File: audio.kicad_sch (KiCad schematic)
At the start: 51 parts, among them J10 Earth, J4 NCJ6FA-H-0, J5 NCJ6FA-H-0, J6 Conn_01x04_Pin, J7 Earth, J8 NCJ6FA-H-0, J9 NCJ6FA-H-0, U5 THAT1246, U6 THAT1246, U7 THAT1646, U8 THAT1646

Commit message: add placement notes into the schematic
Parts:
- D3, D4: Placement (none) -> Near Daisy Seed input. Bottom diode to digital ground.
- JP1: Placement (none) -> As close as possible to Daisy Seed AGND/DGND pins.
- R19, R20: Placement (none) -> In signal path between THAT1246 output and protection diode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
- R21, R23: Placement (none) -> Near 2.5V bias junction, close to signal path.
- R22, R24: Placement (none) -> Near 2.5V bias junction. Bottom resistor, connect to analog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
- R25, R26: Placement (none) -> After 1.2k series resistor in signal path. Ground to analog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
- S1: Placement (none) -> Panel-mounted. Route to signal path with short traces, anal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
- U5, U6: Placement (none) -> Near input connector. Pins 1,4 to analog ground, keep groun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
- U7, U8: Placement (none) -> Near output connector. Analog ground reference.
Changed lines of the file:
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@@
 			)
 		)
+		(property "Placement" "Near Daisy Seed input. Bottom diode to digital ground."
+			(at 118.11 69.85 0)
+			(effects
+				(font
+					(size 1.27 1.27)
+				)
+				(hide yes)
+			)
+		)
 		(pin "1"
 		)
@@
 			)
 		)
+		(property "Placement" "After 1.2k series resistor in signal path. Ground to analog ground."
+			(at 121.92 115.57 0)
+			(effects
+				(font
+					(size 1.27 1.27)
+				)
+				(hide yes)
+			)
+		)
 		(pin "1"
 		)
@@
 			)
 		)
+		(property "Placement" "Near 2.5V bias junction, close to signal path."
+			(at 111.76 60.96 0)
+			(effects
+				(font
+					(size 1.27 1.27)
+				)
+				(hide yes)
+			)
+		)
 		(pin "1"
 		)
@@
 			)
 		)
+		(property "Placement" "Panel-mounted. Route to signal path with short traces, analog ground."
+			(at 86.36 100.33 0)
+			(effects
+				(font
+					(size 1.27 1.27)
+				)
+				(hide yes)
+			)
+		)
 		(pin "1"
 		)
@@
 			)
 		)
+		(property "Placement" "As close as possible to Daisy Seed AGND/DGND pins."
+			(at 229.87 138.43 0)
+			(effects
+				(font
+					(size 1.27 1.27)
+				)
+				(hide yes)
+			)
+		)
 		(pin "2"
 		)
@@
 			)
 		)
+		(property "Placement" "Near input connector. Pins 1,4 to analog ground, keep ground path short and clean."
+			(at 58.42 107.95 0)
+			(effects
+				(font
+					(size 1.27 1.27)
+				)
+				(hide yes)
+			)
+		)
 		(pin "1"
 		)
@@
 			)
 		)
+		(property "Placement" "Near output connector. Analog ground reference."
+			(at 205.74 102.87 0)
+			(effects
+				(font
+					(size 1.27 1.27)
+				)
+				(hide yes)
+			)
+		)
 		(pin "1"
 		)
@@
 			)
 		)
+		(property "Placement" "Near 2.5V bias junction, close to signal path."
+			(at 105.41 60.96 0)
+			(effects
+				(font
+					(size 1.27 1.27)
+				)
+				(hide yes)
+			)
+		)
 		(pin "1"
 		)
@@
 			)
 		)
+		(property "Placement" "Near 2.5V bias junction. Bottom resistor, connect to analog ground."
+			(at 105.41 83.82 0)
+			(effects
+				(font
+					(size 1.27 1.27)
+				)
+				(hide yes)
+			)
+		)
 		(pin "1"
 		)
@@
 			)
 		)
+		(property "Placement" "Near input connector. Pins 1,4 to analog ground, keep ground path short and clean."
+			(at 58.42 45.72 0)
+			(effects
+				(font
+					(size 1.27 1.27)
+				)
+				(hide yes)
+			)
+		)
 		(pin "1"
 		)
@@
 			)
 		)
+		(property "Placement" "Near output connector. Analog ground reference."
+			(at 205.74 40.64 0)
+			(effects
+				(font
+					(size 1.27 1.27)
+				)
+				(hide yes)
+			)
+		)
 		(pin "1"
 		)
@@
 			)
 		)
+		(property "Placement" "In signal path between THAT1246 output and protection diodes."
+			(at 81.28 69.85 0)
+			(effects
+				(font
+					(size 1.27 1.27)
+				)
+				(hide yes)
+			)
+		)
 		(pin "1"
 		)
@@
 			)
 		)
+		(property "Placement" "In signal path between THAT1246 output and protection diodes."
+			(at 81.28 74.93 0)
+			(effects
+				(font
+					(size 1.27 1.27)
+				)
+				(hide yes)
+			)
+		)
 		(pin "1"
 		)
@@
 			)
 		)
+		(property "Placement" "After 1.2k series resistor in signal path. Ground to analog ground."
+			(at 121.92 102.87 0)
+			(effects
+				(font
+					(size 1.27 1.27)
+				)
+				(hide yes)
+			)
+		)
 		(pin "1"
 		)
@@
 			)
 		)
+		(property "Placement" "Near 2.5V bias junction. Bottom resistor, connect to analog ground."
+			(at 111.76 83.82 0)
+			(effects
+				(font
+					(size 1.27 1.27)
+				)
+				(hide yes)
+			)
+		)
 		(pin "1"
 		)
@@
 			(at 125.73 74.93 0)
 			(effects
+				(font
+					(size 1.27 1.27)
+				)
+				(hide yes)
+			)
+		)
+		(property "Placement" "Near Daisy Seed input. Bottom diode to digital ground."
+			(at 125.73 74.93 0)
+			(effects

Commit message: dealing with protection circuit changes
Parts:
- D4: renamed from D3; value BAT54S -> BAV99; symbol Diode:BAT54S -> Diode:BAV99
- D5: renamed from D4; value BAT54S -> BAV99; symbol Diode:BAT54S -> Diode:BAV99
- renumbered D9 to D10, D10 to D11, D11 to D12, D12 to D13, D5 to D6, D6 to D7, D7 to D8, D8 to D9, J9 to J10, J10 to J8, J8 to J9
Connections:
- net AUDIO_IN_L: no longer D4.3 (COM)
- net AUDIO_IN_R: no longer D5.3 (COM)

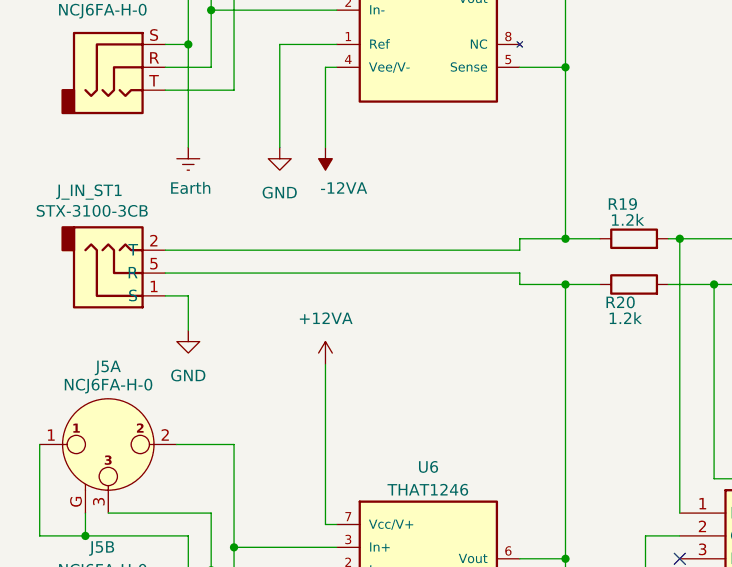
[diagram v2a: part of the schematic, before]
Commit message: deleted 3.55mm input jacks
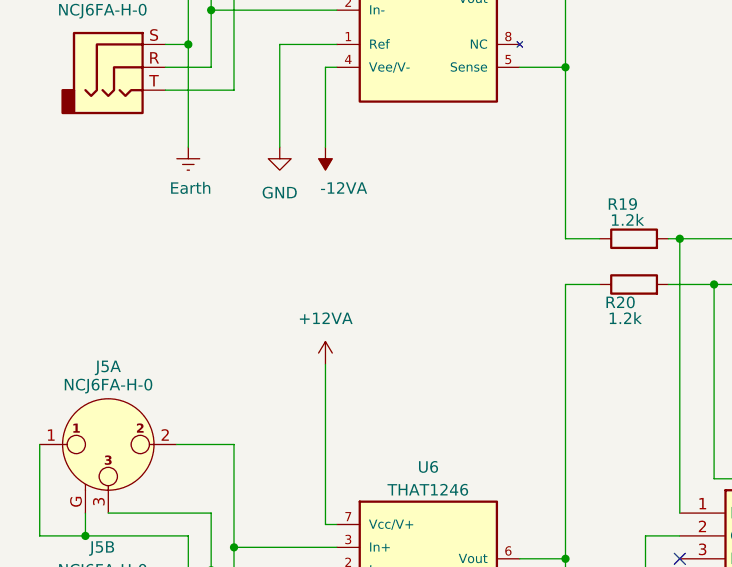
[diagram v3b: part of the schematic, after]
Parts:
- removed J_IN_ST1: STX-3100-3CB, Connector_Audio:Jack_3.5mm_Kycon_STX-3100-3CB, symbol Connector_Audio:AudioJack3
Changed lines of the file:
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@@
 	)
 	(junction
-		(at 73.66 74.93)
-		(diameter 0)
-		(color 0 0 0 0)
-	)
-	(junction
 		(at 184.15 69.85)
 		(diameter 0)
@@
 	)
 	(junction
-		(at 73.66 69.85)
-		(diameter 0)
-		(color 0 0 0 0)
-	)
-	(junction
 		(at 231.14 46.99)
 		(diameter 0)
@@
 	(wire
 		(pts
-			(xy 68.58 69.85) (xy 73.66 69.85)
-		)
-		(stroke
-			(width 0)
-			(type default)
-		)
-	)
-	(wire
-		(pts
 			(xy 43.18 110.49) (xy 43.18 121.92)
 		)
@@
 	(wire
 		(pts
-			(xy 31.75 76.2) (xy 31.75 80.01)
-		)
-		(stroke
-			(width 0)
-			(type default)
-		)
-	)
-	(wire
-		(pts
 			(xy 184.15 41.91) (xy 195.58 41.91)
 		)
@@
 	(wire
 		(pts
-			(xy 29.21 73.66) (xy 68.58 73.66)
-		)
-		(stroke
-			(width 0)
-			(type default)
-		)
-	)
-	(wire
-		(pts
 			(xy 168.91 146.05) (xy 168.91 148.59)
 		)
@@
 	(wire
 		(pts
-			(xy 68.58 71.12) (xy 68.58 69.85)
-		)
-		(stroke
-			(width 0)
-			(type default)
-		)
-	)
-	(wire
-		(pts
 			(xy 215.9 46.99) (xy 220.98 46.99)
 		)
@@
 	(wire
 		(pts
-			(xy 68.58 74.93) (xy 73.66 74.93)
-		)
-		(stroke
-			(width 0)
-			(type default)
-		)
-	)
-	(wire
-		(pts
 			(xy 156.21 35.56) (xy 156.21 40.64)
 		)
@@
 	(wire
 		(pts
-			(xy 68.58 73.66) (xy 68.58 74.93)
-		)
-		(stroke
-			(width 0)
-			(type default)
-		)
-	)
-	(wire
-		(pts
 			(xy 46.99 121.92) (xy 46.99 113.03)
 		)
@@
 	(wire
 		(pts
-			(xy 29.21 76.2) (xy 31.75 76.2)
-		)
-		(stroke
-			(width 0)
-			(type default)
-		)
-	)
-	(wire
-		(pts
 			(xy 15.24 102.87) (xy 20.32 102.87)
 		)
@@
 	(wire
 		(pts
-			(xy 29.21 71.12) (xy 68.58 71.12)
-		)
-		(stroke
-			(width 0)
-			(type default)
-		)
-	)
-	(wire
-		(pts
 			(xy 217.17 138.43) (xy 226.06 138.43)
 		)
@@
 	)
 	(symbol
-		(lib_id "power:GND")
-		(at 31.75 80.01 0)
-		(unit 1)
-		(exclude_from_sim no)
-		(in_bom yes)
-		(on_board yes)
-		(dnp no)
-		(fields_autoplaced yes)
-		(property "Reference" "#PWR030"
-			(at 31.75 86.36 0)
-			(effects
-				(font
-					(size 1.27 1.27)
-				)
-				(hide yes)
-			)
-		)
-		(property "Value" "GND"
-			(at 31.75 85.09 0)
-			(effects
-				(font
-					(size 1.27 1.27)
-				)
-			)
-		)
-		(property "Footprint" ""
-			(at 31.75 80.01 0)
-			(effects
-				(font
-					(size 1.27 1.27)
-				)
-				(hide yes)
-			)
-		)
-		(property "Datasheet" ""
-			(at 31.75 80.01 0)
-			(effects
-				(font
-					(size 1.27 1.27)
-				)
-				(hide yes)
-			)
-		)
-		(property "Description" "Power symbol creates a global label with name \"GND\" , ground"
-			(at 31.75 80.01 0)
-			(effects
-				(font
-					(size 1.27 1.27)
-				)
-				(hide yes)
-			)
-		)
-		(pin "1"
-		)
-		(instances
-			(project "triptech"
-				(path "/55cca6a8-30da-4c13-b2f2-a01401e2b54c/a1b2c3d4-7777-4000-8000-000000000007"
-					(reference "#PWR030")
-					(unit 1)
-				)
-			)
-		)
-	)
-	(symbol
 		(lib_id "Diode:BAV99")
 		(at 118.11 69.85 90)
@@
 					(unit 1)
 				)
-			)
-		)
-	)
-	(symbol
-		(lib_name "AudioJack3_1")
-		(lib_id "Connector_Audio:AudioJack3")
-		(at 24.13 73.66 0)
-		(mirror x)
-		(unit 1)
-		(exclude_from_sim no)
-		(in_bom yes)
-		(on_board yes)
-		(dnp no)
-		(property "Reference" "J_IN_ST1"
-			(at 20.828 64.516 0)
-			(effects
-				(font
-					(size 1.27 1.27)
-				)
-			)
-		)
-		(property "Value" "STX-3100-3CB"
-			(at 21.082 66.802 0)
-			(effects
-				(font
-					(size 1.27 1.27)
-				)
-			)
-		)
-		(property "Footprint" "Connector_Audio:Jack_3.5mm_Kycon_STX-3100-3CB"
-			(at 24.13 73.66 0)
-			(effects
-				(font
-					(size 1.27 1.27)
-				)
-				(hide yes)
-			)
-		)
-		(property "Datasheet" "~"
-			(at 24.13 73.66 0)
-			(effects
-				(font
-					(size 1.27 1.27)
-				)
-				(hide yes)
-			)
-		)
-		(property "Description" "Audio Jack, 3 Poles (Stereo / TRS)"
-			(at 24.13 73.66 0)
-			(effects
-				(font
-					(size 1.27 1.27)
-				)
-				(hide yes)
-			)
-		)
-		(pin "5"
-		)
-		(pin "2"
-		)
-		(pin "1"
-		)
-		(instances
-			(project "triptech"
-				(path "/55cca6a8-30da-4c13-b2f2-a01401e2b54c/a1b2c3d4-7777-4000-8000-000000000007"
-					(reference "J_IN_ST1")
-					(unit 1)
-				)
-			)
-			(project ""
-				(path "/a1b2c3d4-7777-4000-8000-000000000007"
-					(reference "IN_ST1")
-					(unit 1)
-				)

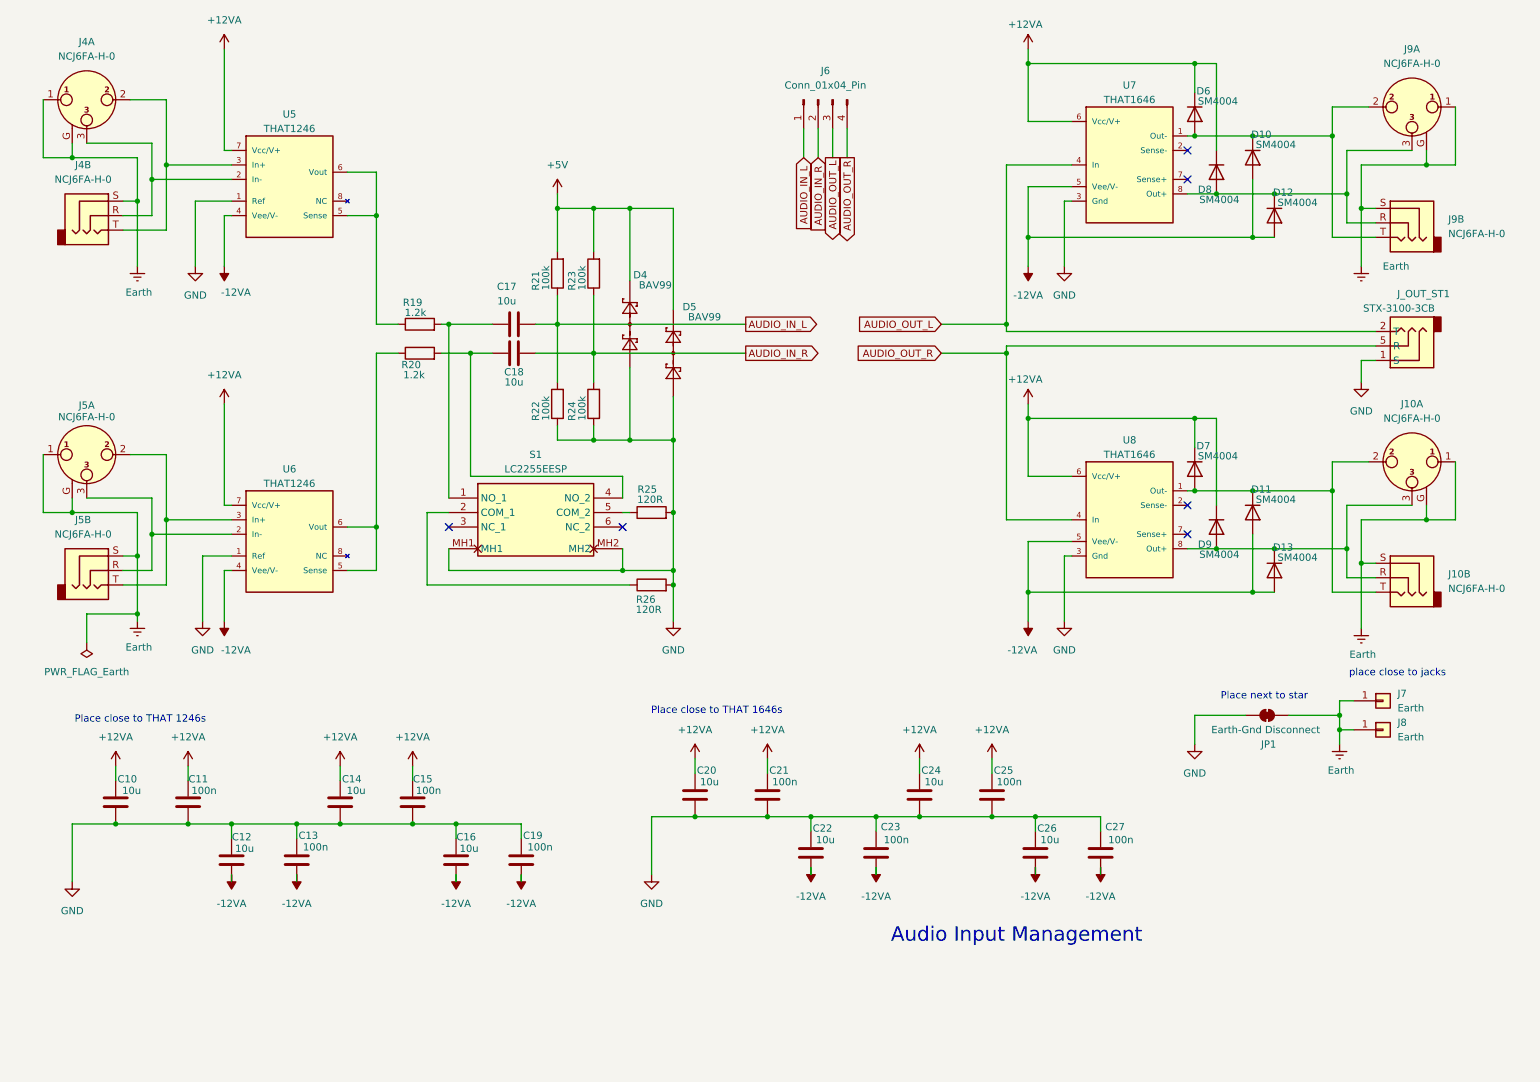
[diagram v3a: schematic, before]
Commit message: audio input for rev 2 laid out in schematic
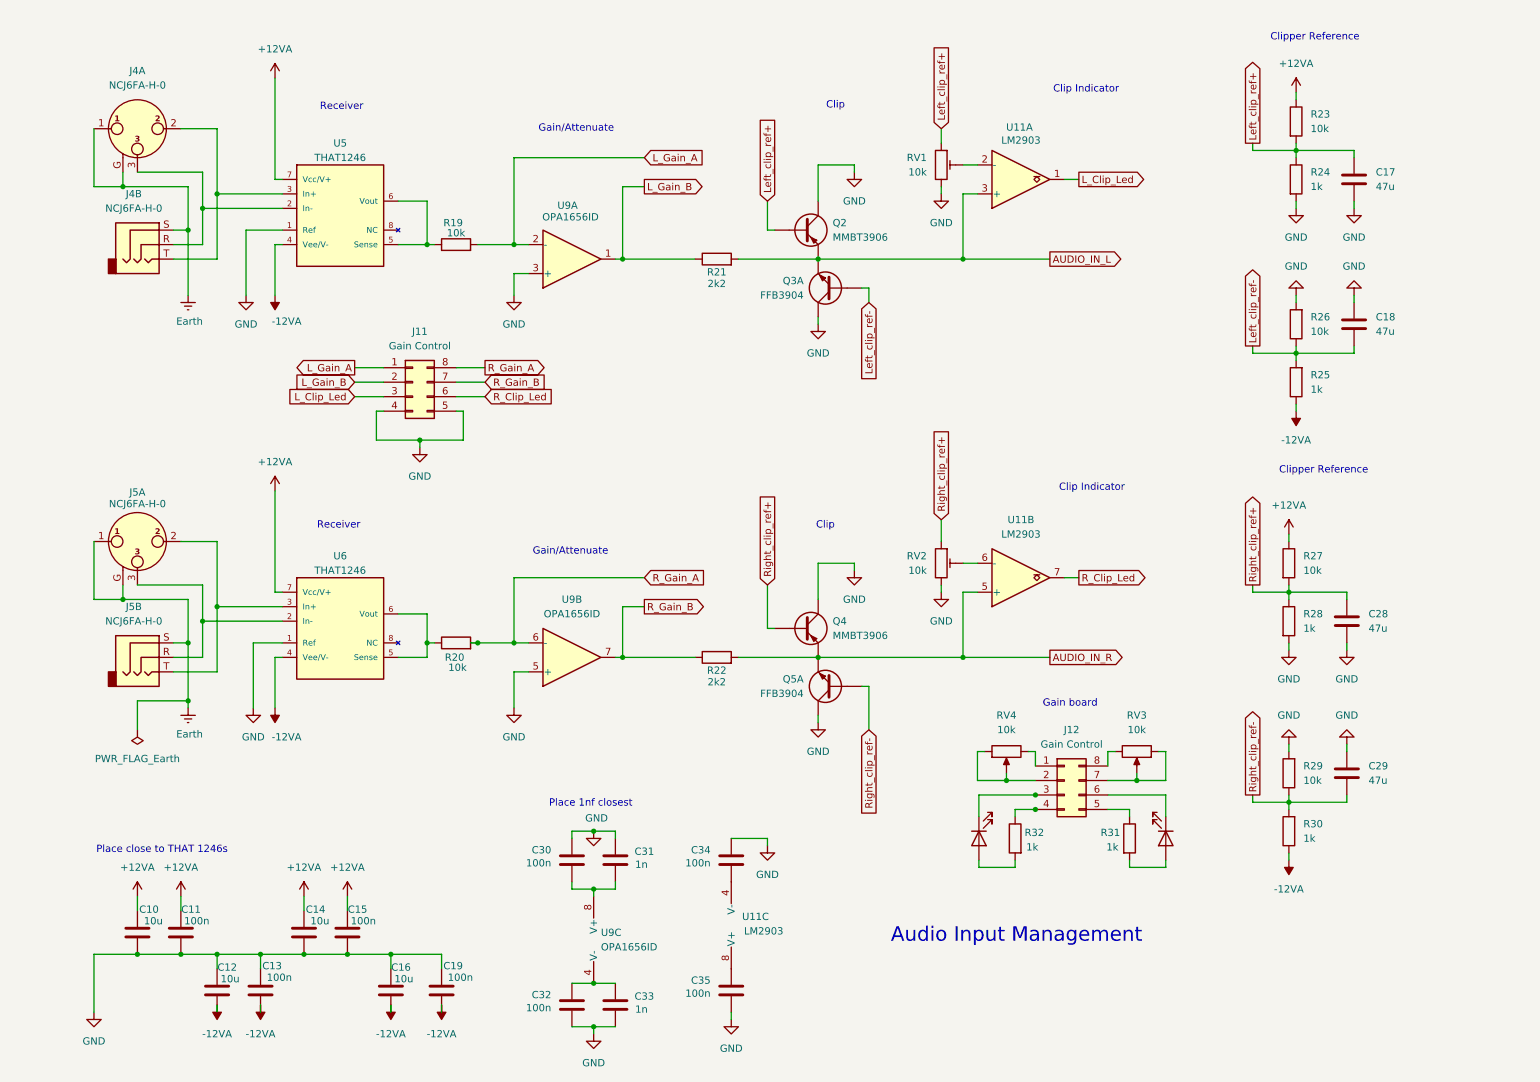
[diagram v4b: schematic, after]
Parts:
- removed C20, C22, C24, C26: 10u, Capacitor_SMD:C_0805_2012Metric, symbol Device:C
- removed C21, C23, C25, C27: 100n, Capacitor_SMD:C_0805_2012Metric, symbol Device:C
- removed D10, D11, D12, D13, D6, D7, D8, D9: SM4004, Diode_SMD:D_SMA, symbol Diode:SM4004
- removed D4, D5: BAV99, Package_TO_SOT_SMD:SOT-23, symbol Diode:BAV99
- removed J10, J9: NCJ6FA-H-0, Connector_Audio:Jack_XLR-6.35mm_Neutrik_NCJ6FA-H-0_Horizontal, symbol Connector_Audio:NCJ6FA-H-0
- removed J6: Conn_01x04_Pin, Connector_PinHeader_2.54mm:PinHeader_1x04_P2.54mm_Vertical, symbol Connector:Conn_01x04_Pin
- removed J7, J8: Earth, MountingHole:MountingHole_3.2mm_M3_Pad_Via, symbol Connector_Generic:Conn_01x01
- removed JP1: Earth-Gnd Disconnect, Jumper:SolderJumper-2_P1.3mm_Bridged_Pad1.0x1.5mm, symbol Jumper:SolderJumper_2_Bridged
- removed J_OUT_ST1: STX-3100-3CB, Connector_Audio:Jack_3.5mm_Kycon_STX-3100-3CB, symbol Connector_Audio:AudioJack3
- removed S1: LC2255EESP, daisy-studio:LC2255EESP, symbol daisy-studio:LC2255EESP
- removed U7, U8: THAT1646, Package_SO:SOIC-8_3.9x4.9mm_P1.27mm, symbol daisy-studio:THAT1646
- added C28, C29: 47u, symbol Device:C
- added C30, C32, C34, C35: 100n, Capacitor_SMD:C_0805_2012Metric, symbol Device:C
- added C31, C33: 1n, Capacitor_SMD:C_0805_2012Metric, symbol Device:C
- added D2, D4: LED, symbol Device:LED
- added J11, J12: Gain Control, symbol Connector_Generic:Conn_02x04_Counter_Clockwise
- added Q2, Q4: MMBT3906, Package_TO_SOT_SMD:SOT-23, symbol Transistor_BJT:MMBT3906
- added Q3, Q5: FFB3904, Package_TO_SOT_SMD:SOT-363_SC-70-6, symbol Transistor_BJT:FFB3904
- added R27, R29: 10k, symbol Device:R
- added R28, R30, R31, R32: 1k, symbol Device:R
- added RV1, RV2: 10k, symbol Device:R_Potentiometer_Trim
- added RV3, RV4: 10k, symbol Device:R_Potentiometer
- added U11: LM2903, symbol Comparator:LM2903
- added U9: OPA1656ID, Package_SO:SOIC-8_3.9x4.9mm_P1.27mm, symbol Amplifier_Operational:OPA1656ID
- C17, C18: value 10u -> 47u; footprint Capacitor_SMD:C_0805_2012Metric -> (none)
- R19, R20: value 1.2k -> 10k
- R21: value 100k -> 2k2; footprint Resistor_SMD:R_0603_1608Metric -> (none); Placement Near 2.5V bias junction, close to signal path. -> (none)
- R22: value 100k -> 2k2; footprint Resistor_SMD:R_0603_1608Metric -> (none); Placement Near 2.5V bias junction. Bottom resistor, connect to analog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 -> (none)
- R23: value 100k -> 10k; footprint Resistor_SMD:R_0603_1608Metric -> (none); Placement Near 2.5V bias junction, close to signal path. -> (none)
- R24: value 100k -> 1k; footprint Resistor_SMD:R_0603_1608Metric -> (none); Placement Near 2.5V bias junction. Bottom resistor, connect to analog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 -> (none)
- R25: value 120R -> 1k; footprint Resistor_SMD:R_0603_1608Metric -> (none); Placement After 1.2k series resistor in signal path. Ground to analog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 -> (none)
- R26: value 120R -> 10k; footprint Resistor_SMD:R_0603_1608Metric -> (none); Placement After 1.2k series resistor in signal path. Ground to analog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 -> (none)
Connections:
- net +12VA: now also R23.1, R27.1
- net -12VA: now also R25.1, R30.1
- net AUDIO_IN_L: now also R21.2, Q2.2 (E), Q3.1 (E1), U11.3 (+); no longer C17.2, R21.1, R22.2
- net AUDIO_IN_R: now also R22.2, Q4.2 (E), Q5.1 (E1), U11.5 (+); no longer C18.2, R23.1, R24.2
- net GND: now also C17.2, C18.1, R24.2, C28.2, C29.1, C30.1, C31.1, C32.2, C33.2, C34.1, C35.2, J11.4 (Pin_4), J11.5 (Pin_5), Q2.3 (C), Q3.6 (C1), Q4.3 (C), Q5.6 (C1), R28.2, R29.2, RV1.3, RV2.3, U9.3 (+), U9.5 (+); no longer R22.1, R24.1, R25.2
- net Left_clip_ref-: now reaches R26.1
- net Left_clip_ref-: now also C18.2, R25.2, Q3.2 (B1)
- net L_Gain_A: now reaches R19.2
- net L_Gain_A: now also J11.1 (Pin_1), U9.2 (-); no longer C17.1
- net R_Gain_A: now reaches R20.2
- net R_Gain_A: now also J11.8 (Pin_8), U9.6 (-); no longer C18.1
- net +5V renamed Left_clip_ref+
- net Left_clip_ref+: now also C17.1, R24.1, Q2.1 (B), RV1.1; no longer R21.2
- new net: RV2.2, U11.6 (-)
- new net: D4.1 (K), J12.3 (Pin_3)
- new net: D4.2 (A), R32.2
- new net: J12.1 (Pin_1), RV4.3
- new net: J12.2 (Pin_2), RV4.1, RV4.2
- new net: J12.4 (Pin_4), R32.1
- new net: J12.5 (Pin_5), R31.1
- new net: D2.1 (K), J12.6 (Pin_6)
- new net: J12.7 (Pin_7), RV3.1, RV3.2
- new net: J12.8 (Pin_8), RV3.3
- new net: D2.2 (A), R31.2
- new net: C32.1, C33.1, U9.4 (V-)
- new net: C30.2, C31.2, U9.8 (V+)
- new net: RV1.2, U11.2 (-)
- new net: C34.2, U11.4 (V-)
- new net: C35.1, U11.8 (V+)
- new net L_Clip_Led: J11.3 (Pin_3), U11.1
- new net L_Gain_B: J11.2 (Pin_2), R21.1, U9.1
- new net R_Clip_Led: J11.6 (Pin_6), U11.7
- new net R_Gain_B: J11.7 (Pin_7), R22.1, U9.7
- new net Right_clip_ref+: C28.1, Q4.1 (B), R27.2, R28.1, RV2.1
- new net Right_clip_ref-: C29.2, Q5.2 (B1), R29.1, R30.2
- no-connect marks 6 -> 0
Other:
- note added: "Clip"
- note added: "Clip Indicator"
- note added: "Clipper Reference"
- note added: "Gain board"
- note added: "Gain/Attenuate"
- note added: "Place 1nf closest"
- note added: "Receiver"
- note removed: "Place close to THAT 1646s"
- note removed: "Place next to star"
- note removed: "place close to jacks"
- title: Triptech Carrier Board - Audio I/O -> Daisy-Studio
- moved on the sheet: C10, C11, C12, C13, C14, C15, C16, C19, J4A, J4B, J5A, J5B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
